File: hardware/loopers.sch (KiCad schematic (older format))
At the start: 0 parts

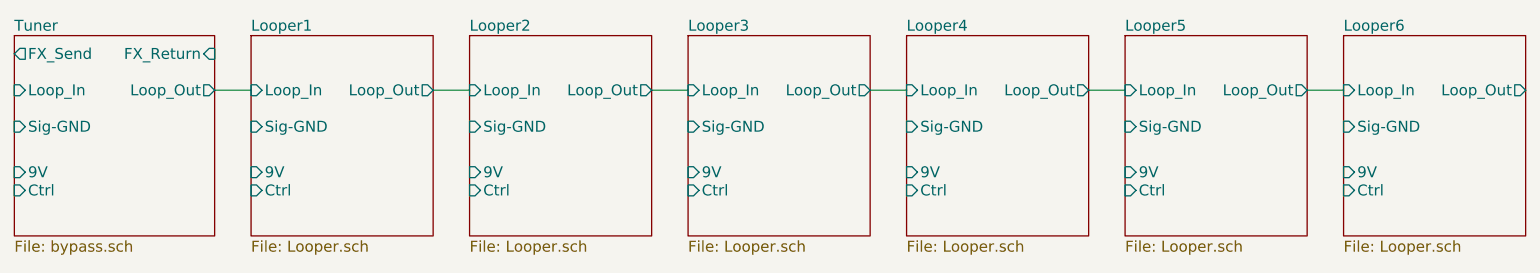
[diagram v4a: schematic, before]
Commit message: Replace Sig-GND label by global GNDA label
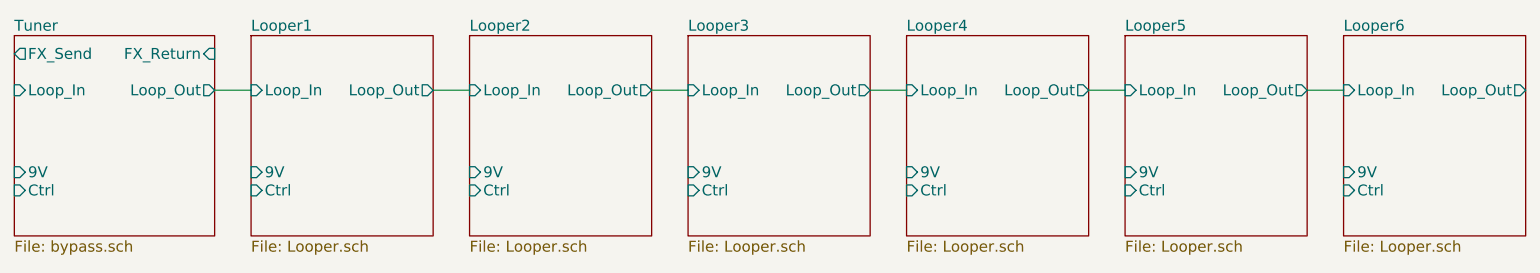
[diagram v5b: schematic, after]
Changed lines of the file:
@@
 F5 "FX_Return" I R 2300 2400 60
 F6 "9V" I L 1200 3050 60
-F7 "Sig-GND" I L 1200 2800 60
-F8 "Ctrl" I L 1200 3150 60
+F7 "Ctrl" I L 1200 3150 60
 $EndSheet
 $Sheet
@@
 F4 "Loop_In" I L 2500 2600 60
 F5 "Loop_Out" O R 3500 2600 60
-F6 "Sig-GND" I L 2500 2800 60
 $EndSheet
 $Sheet
@@
 F4 "Loop_In" I L 3700 2600 60
 F5 "Loop_Out" O R 4700 2600 60
-F6 "Sig-GND" I L 3700 2800 60
 $EndSheet
 $Sheet
@@
 F4 "Loop_In" I L 4900 2600 60
 F5 "Loop_Out" O R 5900 2600 60
-F6 "Sig-GND" I L 4900 2800 60
 $EndSheet
 $Sheet
@@
 F4 "Loop_In" I L 6100 2600 60
 F5 "Loop_Out" O R 7100 2600 60
-F6 "Sig-GND" I L 6100 2800 60
 $EndSheet
 $Sheet
@@
 F4 "Loop_In" I L 7300 2600 60
 F5 "Loop_Out" O R 8300 2600 60
-F6 "Sig-GND" I L 7300 2800 60
 $EndSheet
 $Sheet
@@
 F4 "Loop_In" I L 8500 2600 60
 F5 "Loop_Out" O R 9500 2600 60
-F6 "Sig-GND" I L 8500 2800 60
 $EndSheet
 Wire Wire Line

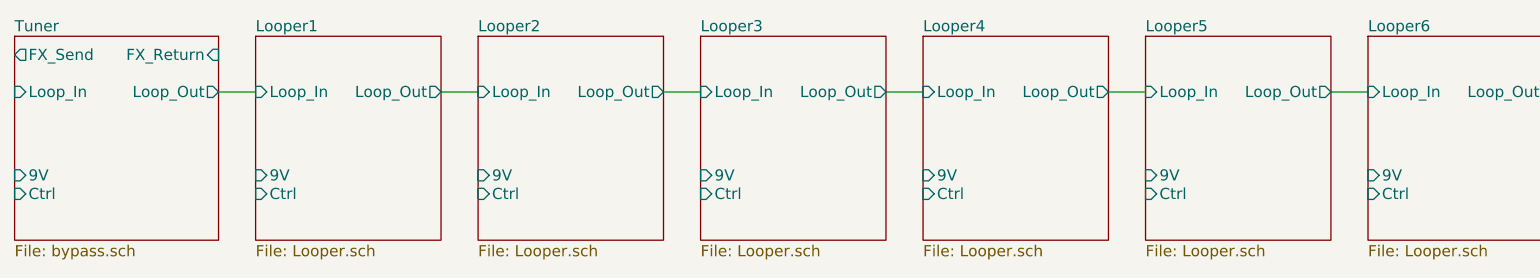
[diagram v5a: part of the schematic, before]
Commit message: Use global label for digital (noisy) 9V
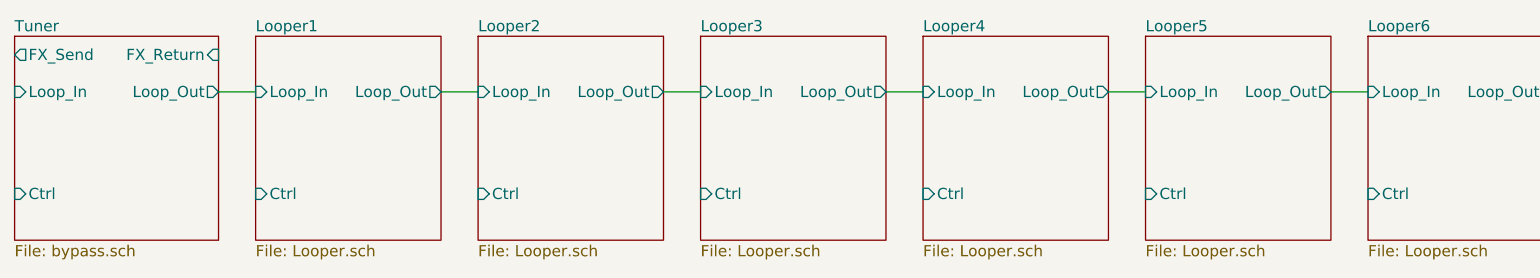
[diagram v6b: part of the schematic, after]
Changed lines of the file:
@@
 F4 "FX_Send" O L 1200 2400 60
 F5 "FX_Return" I R 2300 2400 60
-F6 "9V" I L 1200 3050 60
 F7 "Ctrl" I L 1200 3150 60
 $EndSheet
@@
 F0 "Looper1" 60
 F1 "Looper.sch" 60
-F2 "9V" I L 2500 3050 60
 F3 "Ctrl" I L 2500 3150 60
 F4 "Loop_In" I L 2500 2600 60
@@
 F0 "Looper2" 60
 F1 "Looper.sch" 60
-F2 "9V" I L 3700 3050 60
 F3 "Ctrl" I L 3700 3150 60
 F4 "Loop_In" I L 3700 2600 60
@@
 F0 "Looper3" 60
 F1 "Looper.sch" 60
-F2 "9V" I L 4900 3050 60
 F3 "Ctrl" I L 4900 3150 60
 F4 "Loop_In" I L 4900 2600 60
@@
 F0 "Looper4" 60
 F1 "Looper.sch" 60
-F2 "9V" I L 6100 3050 60
 F3 "Ctrl" I L 6100 3150 60
 F4 "Loop_In" I L 6100 2600 60
@@
 F0 "Looper5" 60
 F1 "Looper.sch" 60
-F2 "9V" I L 7300 3050 60
 F3 "Ctrl" I L 7300 3150 60
 F4 "Loop_In" I L 7300 2600 60
@@
 F0 "Looper6" 60
 F1 "Looper.sch" 60
-F2 "9V" I L 8500 3050 60
 F3 "Ctrl" I L 8500 3150 60
 F4 "Loop_In" I L 8500 2600 60

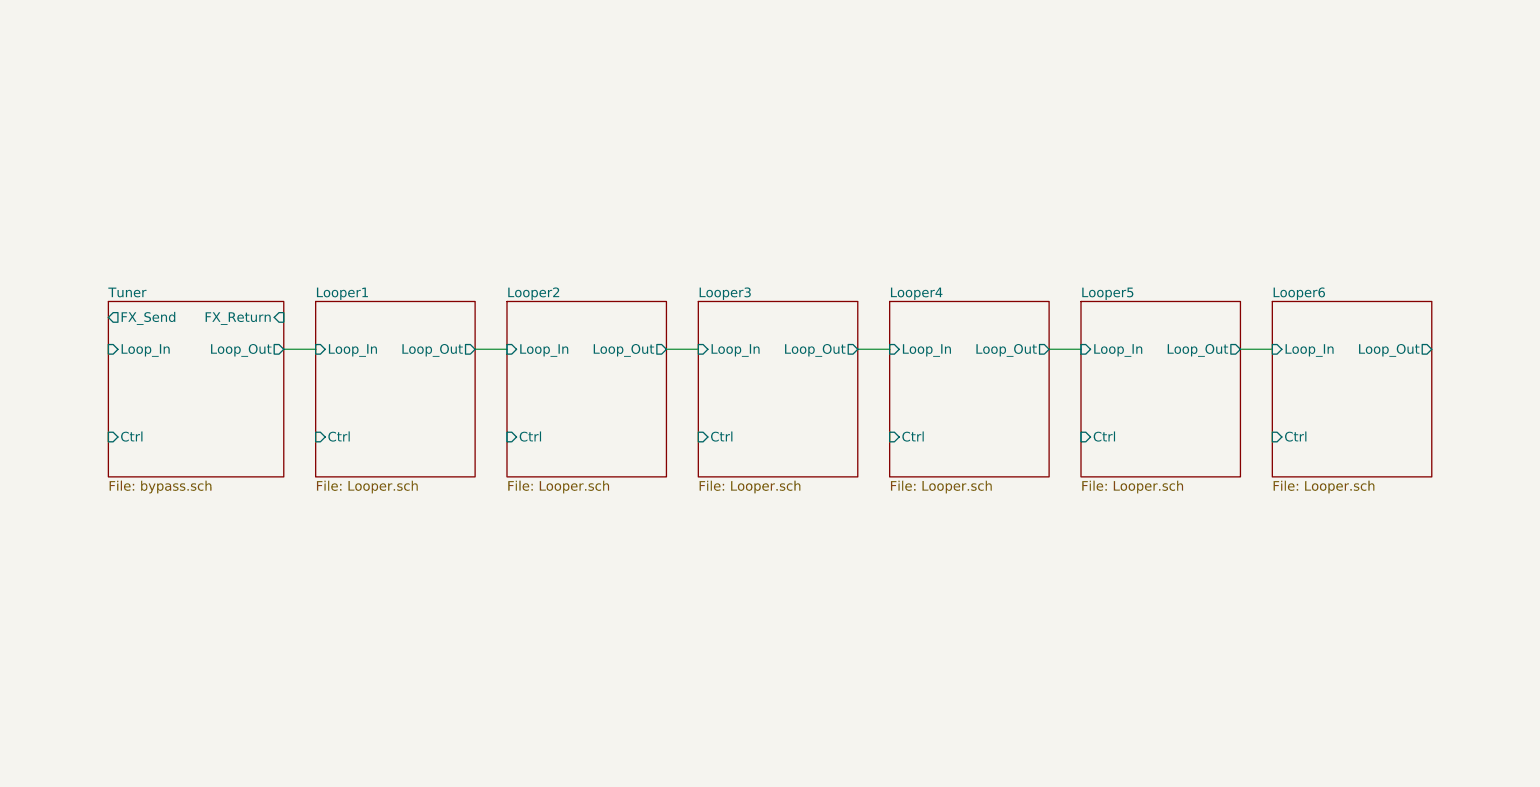
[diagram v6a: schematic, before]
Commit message: Draw looper chain
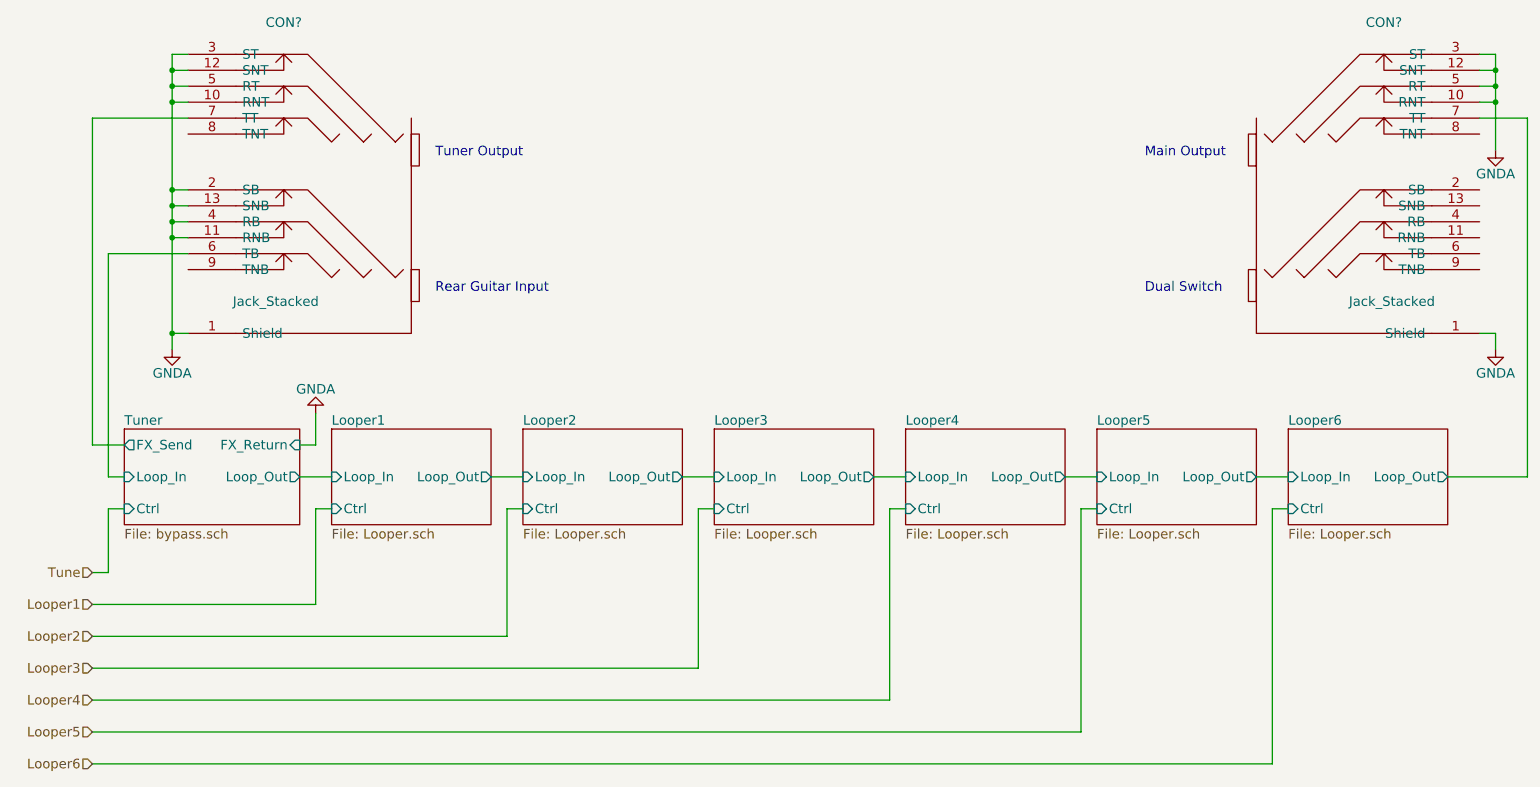
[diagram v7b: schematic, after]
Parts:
- added CON? (x2): Jack_Stacked, symbol Jack_Stacked
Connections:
- net Looper6/Loop_Out: now also CON?.7 (TT)
- net Tuner/FX_Send: now also CON?.7 (TT)
- net Tuner/Loop_In: now also CON?.6 (TB)
- new net GNDA: CON?.1 (Shield), CON?.1 (Shield), CON?.10 (RNT), CON?.10 (RNT), CON?.11 (RNB), CON?.12 (SNT), CON?.12 (SNT), CON?.13 (SNB), CON?.2 (SB), CON?.3 (ST), CON?.3 (ST), CON?.4 (RB), CON?.5 (RT), CON?.5 (RT)
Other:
- note added: "Dual Switch"
- note added: "Main Output"
- note added: "Rear Guitar Input"
- note added: "Tuner Output"
